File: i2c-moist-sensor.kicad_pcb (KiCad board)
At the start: 4 copper layers, 18 x 149 mm, 25 parts, among them IC1 ATTINY441-SSU, P1 CONN_02X03, X1 16MHz

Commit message: fixed unconnected
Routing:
- net GND: track 50.1 -> 53.6 mm, vias 22 -> 23
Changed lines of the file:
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@@
     (thickness 1.6)
     (drawings 20)
-    (tracks 222)
+    (tracks 228)
     (zones 0)
     (modules 25)
@@
   (segment (start 99.25 51.5) (end 99.8 51.5) (width 0.254) (layer F.Cu) (net 2))
   (via (at 99.8 51.5) (size 0.7) (drill 0.4) (layers F.Cu B.Cu) (net 2))
-  (segment (start 87.449997 57.5) (end 87.449997 56.041401) (width 0.254) (layer In1.Cu) (net 2))
   (segment (start 87.449997 56.041401) (end 88.867554 54.623844) (width 0.254) (layer In1.Cu) (net 2))
   (segment (start 88.867554 54.623844) (end 89.558914 54.623844) (width 0.254) (layer In1.Cu) (net 2))
@@
   (segment (start 91.1 47.1) (end 92 48) (width 0.254) (layer In2.Cu) (net 2))
   (via (at 92 48) (size 0.7) (drill 0.4) (layers F.Cu B.Cu) (net 2))
-  (via (at 87.449997 57.3) (size 0.7) (drill 0.4) (layers F.Cu B.Cu) (net 2))
+  (via (at 87.5 56.2) (size 0.7) (drill 0.4) (layers F.Cu B.Cu) (net 2))
   (segment (start 92 54.2) (end 92 57) (width 0.254) (layer In2.Cu) (net 2))
   (segment (start 92 54.2) (end 92 56) (width 0.254) (layer In2.Cu) (net 2))
@@
   (via (at 97.3 55.15) (size 0.7) (drill 0.4) (layers F.Cu B.Cu) (net 2))
   (segment (start 97.268 55.118) (end 97.3 55.15) (width 0.508) (layer F.Cu) (net 2))
-  (segment (start 89.95 34) (end 89.95 33.3) (width 0.508) (layer F.Cu) (net 2))
   (via (at 89.95 33.3) (size 0.7) (drill 0.4) (layers F.Cu B.Cu) (net 2))
   (segment (start 90.15 51.7) (end 90.15 52.4) (width 0.254) (layer F.Cu) (net 2))
   (via (at 90.15 52.4) (size 0.7) (drill 0.4) (layers F.Cu B.Cu) (net 2))
+  (segment (start 89.95 34) (end 89.95 33.3) (width 0.508) (layer F.Cu) (net 2))
+  (segment (start 91.96 54.16) (end 92 54.2) (width 0.254) (layer F.Cu) (net 2))
+  (segment (start 91.96 53.34) (end 91.96 54.16) (width 0.254) (layer F.Cu) (net 2))
+  (via (at 93.027776 34.527776) (size 0.7) (drill 0.4) (layers F.Cu B.Cu) (net 2))
+  (segment (start 93.1 34.6) (end 93.027776 34.527776) (width 0.254) (layer F.Cu) (net 2))
+  (segment (start 93.55 34.6) (end 93.1 34.6) (width 0.254) (layer F.Cu) (net 2))
+  (segment (start 91.8 33.3) (end 89.95 33.3) (width 0.254) (layer In1.Cu) (net 2))
+  (segment (start 93.027776 34.527776) (end 91.8 33.3) (width 0.254) (layer In1.Cu) (net 2))
   (segment (start 88.45 34) (end 88.45 37.60114) (width 0.508) (layer F.Cu) (net 3))
   (segment (start 88.45 37.60114) (end 89 38.15114) (width 0.508) (layer F.Cu) (net 3))
@@
     (polygon
       (pts
-        (xy 97 56.8) (xy 97 95.3) (xy 97 56.8)
+        (xy 97 56.8) (xy 97 95.3)
       )
     )
@@
     (polygon
       (pts
-        (xy 94.6 56.5) (xy 94.5 94.3) (xy 93.8 94.3) (xy 90.5 90.9) (xy 90.5 57.2)
-        (xy 87.1 57.2) (xy 87.2 92.1) (xy 90.1 95) (xy 90.1 148) (xy 93 150.9)
+        (xy 94.6 56.5) (xy 94.5 94.3) (xy 93.8 94.3) (xy 90.5 90.9) (xy 90.5 56.6)
+        (xy 87.1 56.6) (xy 87.2 92.1) (xy 90.1 95) (xy 90.1 148) (xy 93 150.9)
         (xy 97 150.9) (xy 98.5 149.5) (xy 99.9 148.1) (xy 100 94.3) (xy 97.8 94.3)
         (xy 97.8 56.5)

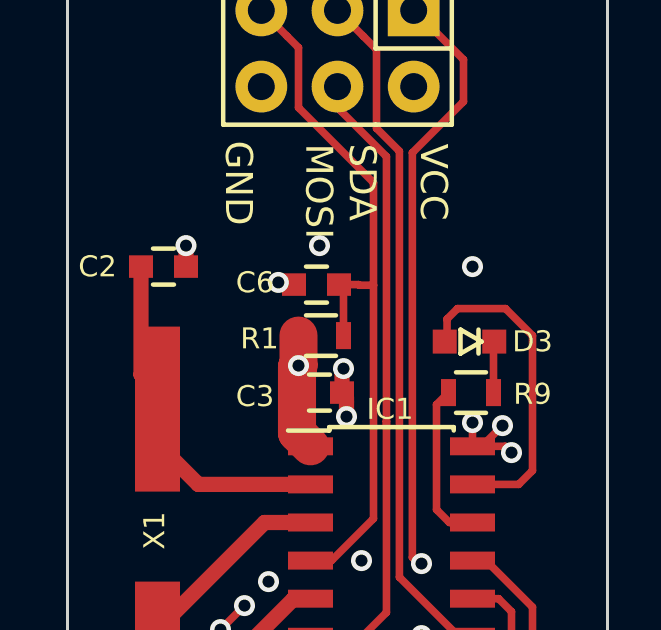
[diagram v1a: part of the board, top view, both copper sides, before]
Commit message: C2||C6
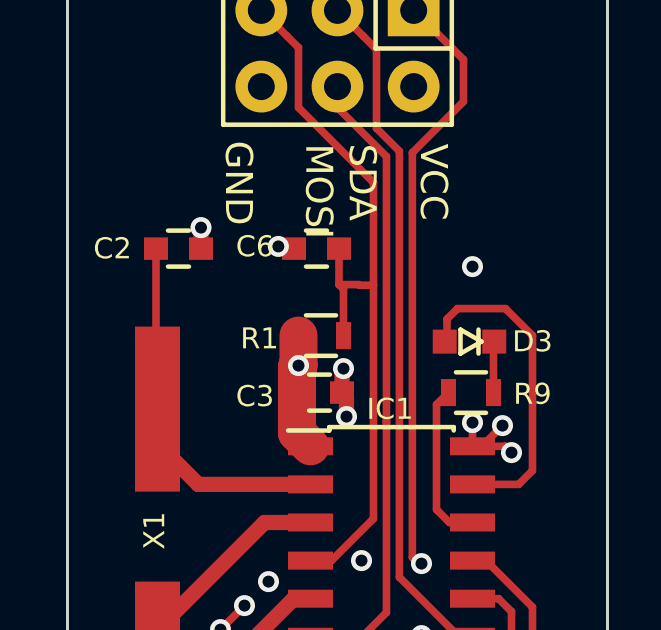
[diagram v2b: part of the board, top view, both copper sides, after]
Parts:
- moved C6 1.20 mm to (94.3, 33.4)
- moved C2 0.78 mm to (89.7, 33.4)
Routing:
- net GND: track 53.6 -> 57.8 mm
- net VCC: track 16.5 -> 15.0 mm, vias 2 -> 1
- net /RESET: track 24.1 -> 25.3 mm
- net Net-(C2-Pad1): track 11.9 -> 12.9 mm
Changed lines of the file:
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@@
   (page A4)
   (layers
-    (0 F.Cu signal)
+    (0 F.Cu signal hide)
     (1 In1.Cu signal)
     (2 In2.Cu signal)
@@
     (35 F.Paste user)
     (36 B.SilkS user hide)
-    (37 F.SilkS user hide)
+    (37 F.SilkS user)
     (38 B.Mask user)
     (39 F.Mask user)
@@
   )
   (module Capacitors_SMD:C_0603 (layer F.Cu)
-    (at 89.2 34)
+    (at 89.7 33.4)
     (descr "Capacitor SMD 0603, reflow soldering, AVX (see smccp.pdf)")
     (tags "capacitor 0603")
@@
   )
   (module Capacitors_SMD:C_0603 (layer F.Cu)
-    (at 94.3 34.6 180)
+    (at 94.3 33.4 180)
     (descr "Capacitor SMD 0603, reflow soldering, AVX (see smccp.pdf)")
     (tags "capacitor 0603")
@@
   (via (at 97.3 55.15) (size 0.7) (drill 0.4) (layers F.Cu B.Cu) (net 2))
   (segment (start 97.268 55.118) (end 97.3 55.15) (width 0.508) (layer F.Cu) (net 2))
-  (via (at 89.95 33.3) (size 0.7) (drill 0.4) (layers F.Cu B.Cu) (net 2))
+  (via (at 90.45 32.7) (size 0.7) (drill 0.4) (layers F.Cu B.Cu) (net 2))
   (segment (start 90.15 51.7) (end 90.15 52.4) (width 0.254) (layer F.Cu) (net 2))
   (via (at 90.15 52.4) (size 0.7) (drill 0.4) (layers F.Cu B.Cu) (net 2))
-  (segment (start 89.95 34) (end 89.95 33.3) (width 0.508) (layer F.Cu) (net 2))
+  (segment (start 90.45 33.4) (end 90.45 32.7) (width 0.508) (layer F.Cu) (net 2))
   (segment (start 91.96 54.16) (end 92 54.2) (width 0.254) (layer F.Cu) (net 2))
   (segment (start 91.96 53.34) (end 91.96 54.16) (width 0.254) (layer F.Cu) (net 2))
-  (via (at 93.027776 34.527776) (size 0.7) (drill 0.4) (layers F.Cu B.Cu) (net 2))
-  (segment (start 93.1 34.6) (end 93.027776 34.527776) (width 0.254) (layer F.Cu) (net 2))
-  (segment (start 93.55 34.6) (end 93.1 34.6) (width 0.254) (layer F.Cu) (net 2))
-  (segment (start 91.8 33.3) (end 89.95 33.3) (width 0.254) (layer In1.Cu) (net 2))
-  (segment (start 93.027776 34.527776) (end 91.8 33.3) (width 0.254) (layer In1.Cu) (net 2))
-  (segment (start 88.45 34) (end 88.45 37.60114) (width 0.508) (layer F.Cu) (net 3))
-  (segment (start 88.45 37.60114) (end 89 38.15114) (width 0.508) (layer F.Cu) (net 3))
+  (via (at 93.027776 33.327776) (size 0.7) (drill 0.4) (layers F.Cu B.Cu) (net 2))
+  (segment (start 93.1 33.4) (end 93.027776 33.327776) (width 0.254) (layer F.Cu) (net 2))
+  (segment (start 93.55 33.4) (end 93.1 33.4) (width 0.254) (layer F.Cu) (net 2))
+  (segment (start 91.077776 33.327776) (end 90.45 32.7) (width 0.254) (layer In1.Cu) (net 2))
+  (segment (start 93.027776 33.327776) (end 91.077776 33.327776) (width 0.254) (layer In1.Cu) (net 2))
+  (segment (start 93.027776 35.227776) (end 95.2 37.4) (width 0.254) (layer In1.Cu) (net 2))
+  (segment (start 93.027776 33.327776) (end 93.027776 35.227776) (width 0.254) (layer In1.Cu) (net 2))
   (segment (start 94.1 41.26) (end 90.3588 41.26) (width 0.508) (layer F.Cu) (net 3))
   (segment (start 90.3588 41.26) (end 89 39.9012) (width 0.508) (layer F.Cu) (net 3))
   (segment (start 89 39.9012) (end 89 38.15114) (width 0.508) (layer F.Cu) (net 3))
   (segment (start 89.06886 38.22) (end 89 38.15114) (width 0.254) (layer F.Cu) (net 3))
+  (segment (start 88.95 38.7) (end 89 38.75) (width 0.254) (layer F.Cu) (net 3))
+  (segment (start 88.95 33.4) (end 88.95 38.7) (width 0.254) (layer F.Cu) (net 3))
   (segment (start 95.846688 33.353312) (end 93.7 35.5) (width 1.27) (layer In2.Cu) (net 4))
   (segment (start 97.54 31.66) (end 95.846688 33.353312) (width 1.27) (layer In2.Cu) (net 4))
-  (segment (start 95.846688 33.353312) (end 94.453312 33.353312) (width 0.508) (layer In2.Cu) (net 4))
-  (segment (start 94.453312 33.353312) (end 94.4 33.3) (width 0.508) (layer In2.Cu) (net 4))
-  (via (at 94.4 33.3) (size 0.7) (drill 0.4) (layers F.Cu B.Cu) (net 4))
   (segment (start 97.54 28) (end 97.54 31.66) (width 1.27) (layer In2.Cu) (net 4))
   (segment (start 93.7 35.5) (end 93.7 37.3) (width 1.27) (layer In2.Cu) (net 4))
@@
   (segment (start 95.2 36.3) (end 95.2 34.75) (width 0.254) (layer F.Cu) (net 8))
   (segment (start 95.2 34.75) (end 95.05 34.6) (width 0.254) (layer F.Cu) (net 8))
+  (segment (start 95.05 33.4) (end 95.05 34.6) (width 0.254) (layer F.Cu) (net 8))
   (segment (start 90.25 55.749996) (end 90.25 56.75) (width 0.508) (layer F.Cu) (net 9))
   (segment (start 90.599999 55.399997) (end 90.25 55.749996) (width 0.508) (layer In2.Cu) (net 9))

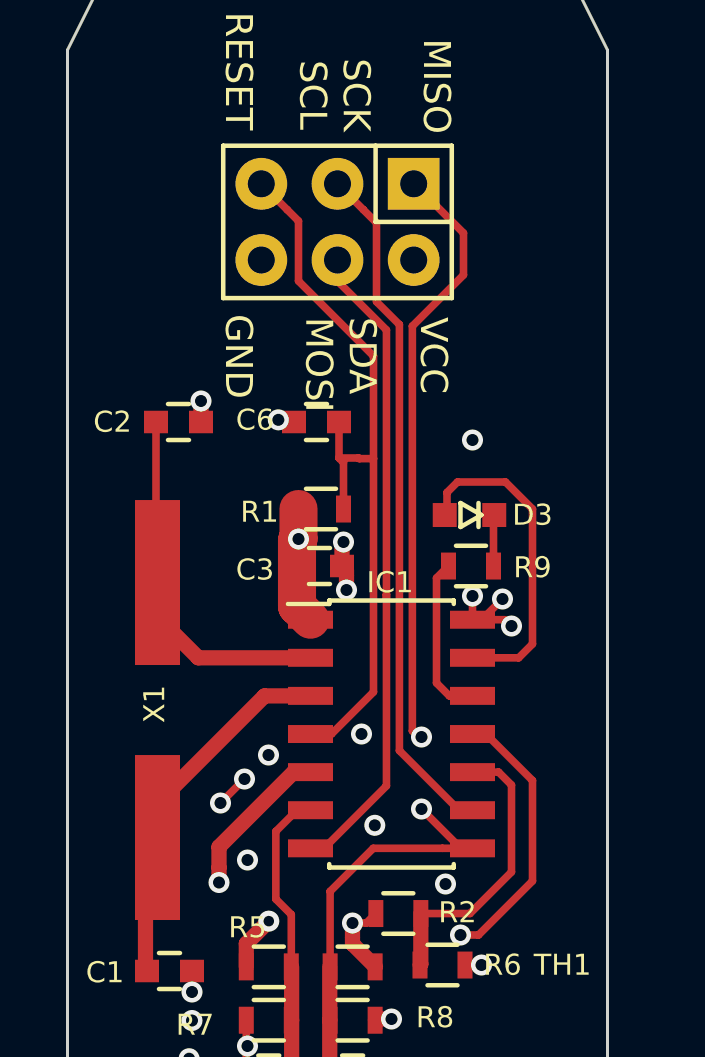
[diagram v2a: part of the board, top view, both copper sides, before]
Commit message: new header, connected SENSE-HIGH, RESET, GND
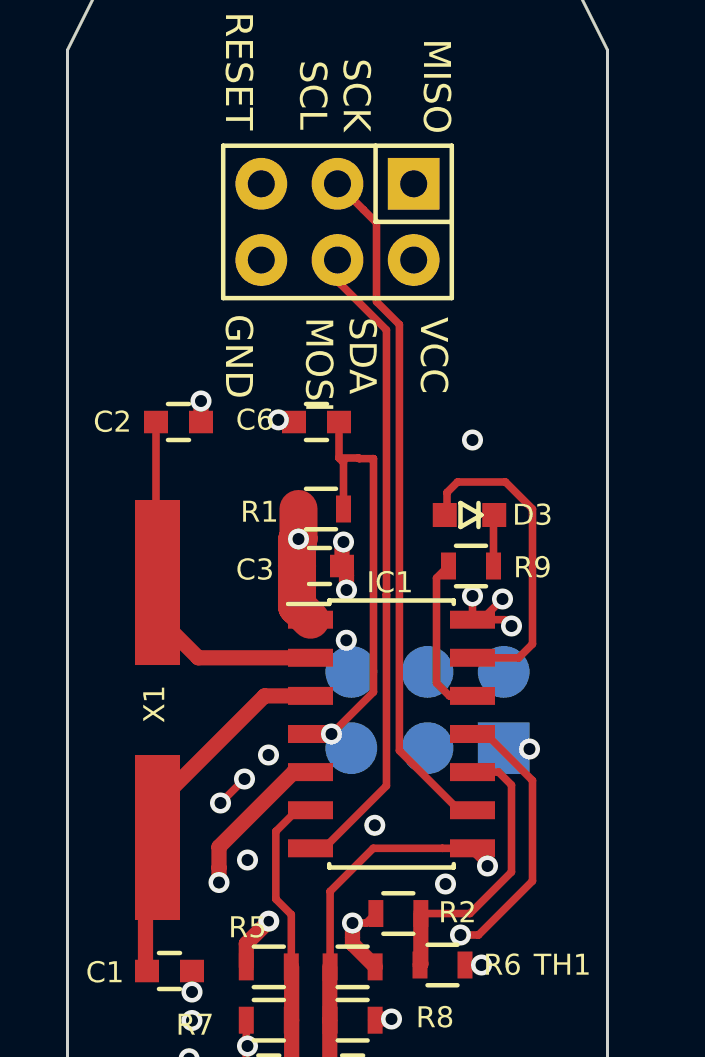
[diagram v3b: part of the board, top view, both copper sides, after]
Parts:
- added P1: CONN_02X03, programming_header:Pin_Header_Straight_2x03, B.Cu at (98.0, 43.0)
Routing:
- net /MISO/SENSE_HIGH: track 38.1 -> 20.0 mm
- net /RESET: track 25.3 -> 14.6 mm, vias 0 -> 1
- net GND: track 57.8 -> 59.0 mm
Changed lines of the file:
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@@
     (thickness 1.6)
     (drawings 20)
-    (tracks 228)
+    (tracks 225)
     (zones 0)
-    (modules 25)
+    (modules 26)
     (nets 17)
   )
   (page A4)
   (layers
-    (0 F.Cu signal hide)
+    (0 F.Cu signal)
     (1 In1.Cu signal)
     (2 In2.Cu signal)
@@
     (mod_text_size 0.7 0.7)
     (mod_text_width 0.11)
-    (pad_size 0.6 1.14)
+    (pad_size 1.7272 1.7272)
     (pad_drill 0)
     (pad_to_mask_clearance 0)
@@
       (xy 18.376834 -6.315505) (xy 18.387358 -6.35) (xy 18.451288 -6.557312) (xy 18.477643 -6.43786)) (layer B.SilkS) (width 0.01))
   )
+  (module programming_header:Pin_Header_Straight_2x03 (layer B.Cu)
+    (at 98 43 180)
+    (descr "Through hole pin header")
+    (tags "pin header")
+    (fp_text reference P1 (at 0 3.81 180) (layer B.SilkS) hide
+      (effects (font (size 0.7 0.7) (thickness 0.11)) (justify mirror))
+    )
+    (fp_text value CONN_02X03 (at 0.25 -3) (layer B.SilkS)
+      (effects (font (size 0.7 0.7) (thickness 0.11)) (justify mirror))
+    )
+    (pad 6 smd circle (at 2.54 1.27 180) (size 1.7272 1.7272) (layers B.Cu B.Paste B.Mask)
+      (net 2 GND))
+    (pad 5 smd circle (at 2.54 -1.27 180) (size 1.7272 1.7272) (layers B.Cu B.Paste B.Mask)
+      (net 8 /RESET))
+    (pad 4 smd circle (at 0 1.27 180) (size 1.7272 1.7272) (layers B.Cu B.Paste B.Mask)
+      (net 13 /MOSI/SDA))
+    (pad 3 smd circle (at 0 -1.27 180) (size 1.7272 1.7272) (layers B.Cu B.Paste B.Mask)
+      (net 12 /SCK/SCL))
+    (pad 2 smd circle (at -2.54 1.27 180) (size 1.7272 1.7272) (layers B.Cu B.Paste B.Mask)
+      (net 4 VCC))
+    (pad 1 smd rect (at -2.54 -1.27 180) (size 1.7272 1.7272) (layers B.Cu B.Paste B.Mask)
+      (net 14 /MISO/SENSE_HIGH))
+  )
   (dimension 18 (width 0.175) (layer Cmts.User)
     (gr_text "18,000 mm" (at 95 162.7) (layer Cmts.User)
@@
   (segment (start 95.8 46.4) (end 96.243021 46.843021) (width 0.254) (layer In2.Cu) (net 2))
   (via (at 96.243021 46.843021) (size 0.7) (drill 0.4) (layers F.Cu B.Cu) (net 2))
-  (segment (start 95.3 39) (end 95.3 43.3) (width 0.254) (layer In2.Cu) (net 2))
   (segment (start 95.3 43.3) (end 95.8 43.8) (width 0.254) (layer In2.Cu) (net 2))
-  (via (at 95.8 43.8) (size 0.7) (drill 0.4) (layers F.Cu B.Cu) (net 2))
   (segment (start 91.9 45.3) (end 92.7 44.5) (width 0.254) (layer In2.Cu) (net 2))
   (via (at 92.7 44.5) (size 0.7) (drill 0.4) (layers F.Cu B.Cu) (net 2))
@@
   (segment (start 93.027776 35.227776) (end 95.2 37.4) (width 0.254) (layer In1.Cu) (net 2))
   (segment (start 93.027776 33.327776) (end 93.027776 35.227776) (width 0.254) (layer In1.Cu) (net 2))
+  (segment (start 95.3 39) (end 95.3 43.3) (width 0.254) (layer In2.Cu) (net 2))
+  (via (at 95.294552 40.675487) (size 0.7) (drill 0.4) (layers F.Cu B.Cu) (net 2))
+  (segment (start 95.46 40.840935) (end 95.294552 40.675487) (width 0.254) (layer B.Cu) (net 2))
+  (segment (start 95.46 41.73) (end 95.46 40.840935) (width 0.254) (layer B.Cu) (net 2))
   (segment (start 94.1 41.26) (end 90.3588 41.26) (width 0.508) (layer F.Cu) (net 3))
   (segment (start 90.3588 41.26) (end 89 39.9012) (width 0.508) (layer F.Cu) (net 3))
@@
   (segment (start 94.8 43.8) (end 96.2 42.4) (width 0.254) (layer F.Cu) (net 8))
   (segment (start 96.2 42.4) (end 96.2 34.621178) (width 0.254) (layer F.Cu) (net 8))
-  (segment (start 96.2 34.621178) (end 96.2 31.2) (width 0.254) (layer F.Cu) (net 8))
-  (segment (start 96.2 31.2) (end 93.7 28.7) (width 0.254) (layer F.Cu) (net 8))
-  (segment (start 93.7 28.7) (end 93.7 26.7) (width 0.254) (layer F.Cu) (net 8))
-  (segment (start 93.7 26.7) (end 93.323599 26.323599) (width 0.254) (layer F.Cu) (net 8))
-  (segment (start 93.323599 26.323599) (end 92.46 25.46) (width 0.254) (layer F.Cu) (net 8))
   (segment (start 95.05 34.6) (end 95.704 34.6) (width 0.254) (layer F.Cu) (net 8))
   (segment (start 95.704 34.6) (end 95.725178 34.621178) (width 0.254) (layer F.Cu) (net 8))
@@
   (segment (start 95.2 34.75) (end 95.05 34.6) (width 0.254) (layer F.Cu) (net 8))
   (segment (start 95.05 33.4) (end 95.05 34.6) (width 0.254) (layer F.Cu) (net 8))
+  (segment (start 94.8 43.8) (end 94.8 43.8) (width 0.254) (layer F.Cu) (net 8))
+  (via (at 94.8 43.8) (size 0.7) (drill 0.4) (layers F.Cu B.Cu) (net 8))
   (segment (start 90.25 55.749996) (end 90.25 56.75) (width 0.508) (layer F.Cu) (net 9))
   (segment (start 90.599999 55.399997) (end 90.25 55.749996) (width 0.508) (layer In2.Cu) (net 9))
@@
   (segment (start 96.63181 39.151337) (end 96.63181 45.52819) (width 0.254) (layer F.Cu) (net 13))
   (segment (start 96.63181 39.278861) (end 96.63181 39.151337) (width 0.254) (layer F.Cu) (net 13))
-  (segment (start 97.8 43.9) (end 97.7 43.9) (width 0.254) (layer F.Cu) (net 14))
-  (segment (start 97.49543 30.20457) (end 99.2 28.5) (width 0.254) (layer F.Cu) (net 14))
-  (segment (start 97.7 43.9) (end 97.49543 43.69543) (width 0.254) (layer F.Cu) (net 14))
-  (segment (start 97.49543 43.69543) (end 97.49543 30.20457) (width 0.254) (layer F.Cu) (net 14))
-  (segment (start 99.2 28.5) (end 99.2 27.1) (width 0.254) (layer F.Cu) (net 14))
-  (segment (start 99.2 27.1) (end 97.56 25.46) (width 0.254) (layer F.Cu) (net 14))
   (segment (start 97.56 25.46) (end 97.54 25.46) (width 0.254) (layer F.Cu) (net 14))
   (segment (start 94.754 51.562) (end 94.754 49.046) (width 0.254) (layer F.Cu) (net 14))
@@
   (segment (start 94.742 55.118) (end 94.742 53.34) (width 0.508) (layer F.Cu) (net 14))
   (segment (start 94.742 53.34) (end 94.742 51.562) (width 0.508) (layer F.Cu) (net 14))
-  (via (at 97.8 43.9) (size 0.7) (drill 0.4) (layers F.Cu B.Cu) (net 14))
-  (via (at 97.8 46.3) (size 0.7) (drill 0.4) (layers F.Cu B.Cu) (net 14))
-  (segment (start 97.8 43.9) (end 97.8 46.3) (width 0.254) (layer In2.Cu) (net 14))
+  (via (at 101.4 44.3) (size 0.7) (drill 0.4) (layers F.Cu B.Cu) (net 14))
+  (via (at 100 48.2) (size 0.7) (drill 0.4) (layers F.Cu B.Cu) (net 14))
   (segment (start 99.11 47.61) (end 99.5 47.61) (width 0.254) (layer F.Cu) (net 14))
-  (segment (start 97.8 46.3) (end 99.11 47.61) (width 0.254) (layer F.Cu) (net 14))
+  (segment (start 101.37 44.27) (end 101.4 44.3) (width 0.254) (layer B.Cu) (net 14))
+  (segment (start 100.54 44.27) (end 101.37 44.27) (width 0.254) (layer B.Cu) (net 14))
+  (segment (start 99.5 47.7) (end 100 48.2) (width 0.254) (layer F.Cu) (net 14))
+  (segment (start 99.5 47.61) (end 99.5 47.7) (width 0.254) (layer F.Cu) (net 14))
+  (segment (start 101.4 46.8) (end 101.4 44.3) (width 0.254) (layer In2.Cu) (net 14))
+  (segment (start 100 48.2) (end 101.4 46.8) (width 0.254) (layer In2.Cu) (net 14))
   (segment (start 95.5 50.1) (end 95.962 50.1) (width 0.254) (layer F.Cu) (net 15))
   (segment (start 95.962 50.1) (end 96.278 49.784) (width 0.254) (layer F.Cu) (net 15))

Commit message: new header
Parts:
- removed the P1 at (95.0, 26.7)
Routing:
- net /SCK/SCL: track 23.0 -> 3.35 mm, vias 0 -> 1
- net /MOSI/SDA: track 21.7 -> 7.78 mm, vias 0 -> 1
- net VCC: track 15.0 -> 13.9 mm, vias 1 -> 3
- net GND: track 59.0 -> 57.8 mm
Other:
- board text removed: "GND"
- board text removed: "MISO"
- board text removed: "RESET"
- board text removed: "SCK SCL"
- board text removed: "SDA MOSI"
- board text removed: "VCC"
